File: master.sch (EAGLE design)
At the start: 27 parts, among them IC1 MEGA164/324/644/1284, SW1 CI-11, U2 3V3 something

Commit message: added forgotten lan interface
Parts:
- removed DHT22: FE04-1, con-lsta:FE04-1
- removed JP1: AVR-ISP-6VERT, avr-7:AVR-ISP-6VERT
- removed NRF24L01: (no value), con-lsta:FE05-2
- removed S1, S3: (no value), switch-omron:10-XX
- removed U$1: BTHQ24008VSS, lcd_displays:BTHQ24008VSS
- removed U2: 3V3 something, asko:MCP1702-5002
- added C10, C11, C12, C17, C18, C19, C20, C21, C4, C5, C6, C9: 100n, rcl:C-EUC0603
- added C13, C15: 10n, rcl:C-EUC0603
- added C14: .22, carrilib:SUPERCAP
- added C16: 10u, rcl:C-EUC0603
- added C22, C23: 22p, rcl:C-EUC0603
- added D1: BAS40-04, diode:BAS40-04
- added IC2: MCP1703-3302, karlnet-parts:MCP1700SOT89
- added IC3: ENC28J60SO, microchip:ENC28J60SO
- added L2: 10u, inductor-neosid:SM-NE29
- added LAN1: MAGJACK, magjack:MAGJACK
- added LCD1: LCD, external:LCD
- added M1: DHT22-NP, modules:DHT22-NP
- added M2: NRF24L01P-M, modules:NRF24L01P-M
- added PDI: AVR-PDIVERT, avr-7:AVR-PDIVERT
- added Q2: IRLML2502, mosfet:IRLML2502
- added Q3: 25MHz, crystal:CRYSTALHC49S
- added R10, R12: 49R9, rcl:R-EU_R0603
- added R11: 4k7, rcl:R-EU_R0603
- added R13: 2k, rcl:R-EU_R0603
- added R14, R15: 100, rcl:R-EU_R0603
- added R9: 10K, rcl:R-EU_R0603
- added U1: 25LC640A-E/SN, microchip:25LC640A-E/SN
- added UC1: XMEGA-A3TQFP, avr-7:XMEGA-A3TQFP
- added X1: serial, pinhead-mod:PINHD-1X4_2.54
- added X2: SPI/1W, con-amp-micromatch:MICROMATCH-8
- added X3: I2C, con-amp-micromatch:MICROMATCH-4
- added X4: ADC, con-amp-micromatch:MICROMATCH-8
- added X5: (no value), con-usb:USB-MB-S
- added X6, X7, X8, X9: PS25_3W-R, con_PS25:PS25_3W-R
- C1, C2, C3, C7, C8: device rcl:C-EUC0805 -> rcl:C-EUC0603
- IC1: value MEGA164/324/644/1284 -> DS1302SOIC; device avr-7:MEGA164P/324P/644P-PU -> adafruit:DS1302SOIC
- R1, R2, R4, R5: device rcl:R-EU_R0805 -> rcl:R-EU_R0603
- R3: value 10k -> 10K; device pot:TRIM_EU-ST10 -> rcl:R-EU_R0603
- R6, R7: value 4k7 -> 49R9; device rcl:R-EU_0207/7 -> rcl:R-EU_R0603
- R8: device rcl:R-EU_0207/7 -> rcl:R-EU_R0603
- S2: device switch-omron:10-XX -> jt-switches:MEC-SWITCHSMT
- SG1: value EFBAA40D101 -> RMP-14SP; device buzzer:EFBAA40D101 -> buzzer:F/CM12P
- SW1: value CI-11 -> EC12E_SW; device piher:CI-11 -> switch-alps:EC12E_SW
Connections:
- removed net !RESET: IC1.!RESET, JP1.5, R1.1
- removed net +3V3: C8.1, NRF24L01.10, NRF24L01.9, U2.OUT
- removed net PA0: IC1.(ADC0/PCINT0)PA0, U$1.RS
- removed net PA1: IC1.(ADC1/PCINT1)PA1, U$1.R/W
- removed net PA2: IC1.(ADC2/PCINT2)PA2, U$1.E
- removed net PA3: IC1.(ADC3/PCINT3)PA3, U$1.DB4
- removed net PA4: IC1.(ADC4/PCINT4)PA4, U$1.DB5
- removed net PA5: IC1.(ADC5/PCINT5)PA5, U$1.DB6
- removed net PA6: IC1.(ADC6/PCINT6)PA6, U$1.DB7
- removed net PA7: IC1.(ADC7/PCINT7)PA7, SG1.1
- removed net PB0: IC1.(XCK0/T0/PCINT8)PB0, R4.1
- removed net PB1: IC1.(CLKO/T1/PCINT9)PB1, R5.1
- removed net PB2: IC1.(INT2/AIN0/PCINT10)PB2, NRF24L01.4
- removed net PB3: IC1.(OC0A/AIN1/PCINT11)PB3, JP1.4, NRF24L01.7
- removed net PB4: IC1.(OC0B/!SS!/PCINT12)PB4, JP1.1, NRF24L01.8
- removed net PB5: IC1.(MOSI/PCINT13)PB5, JP1.3, R8.2
- removed net PB6: IC1.(MISO/PCINT14)PB6, R7.1
- removed net PB7: IC1.(SCK/PCINT15)PB7, R6.1
- removed net PC0: IC1.(SCL/PCINT16)PC0, SW1A.B
- removed net PC1: IC1.(SDA/PCINT17)PC1, SW1A.A
- removed net PC2: IC1.(TCK/PCINT18)PC2, SW1B.D
- removed net PC3: IC1.(TMS/PCINT19)PC3, S1.P
- removed net PC4: IC1.(TDO/PCINT20)PC4, S2.P
- removed net PC5: IC1.(TDI/PCINT21)PC5, S3.P
- removed net PD5: IC1.(OC1A/PCINT29)PD5, U$1.K
- removed net PD6: DHT22.2, IC1.(OC2B/ICP/PCINT30)PD6, R2.2
- new net !EEPCS: U1.!CS, UC1.PF0(OC0A)
- new net !EEPHOLD: U1.!HOLD, UC1.PF1(OC0B/XCK0)
- new net !LANCS: IC3.!CS, UC1.PC6(MISO/RXD1)
- new net !LANINT: IC3.!INT, UC1.PC5(OC1B/MOSI/XCK1)
- new net !RFCS: M2.!CS, UC1.PD1(OC0B/XCK0)
- new net ADC0: UC1.PA0(ADC0/AREFA), X4-2.S
- new net ADC1: UC1.PA1(ADC1), X4-3.S
- new net ADC2: UC1.PA2(ADC2), X4-4.S
- new net ADC3: UC1.PA3(ADC3), X4-5.S
- new net ADC4: UC1.PA4(ADC4), X4-6.S
- new net ADC5: UC1.PA5(ADC5), X4-7.S
- new net BUZZ: SG1.1, UC1.PF7
- new net DHTDATA: M1.DATA, R2.1, UC1.PA7/(ADC7/AC0-OUT)
- new net LCD_BGLED: Q2.G, R9.1, UC1.PC1(OC0B/XCK0/SCL)
- new net LCD_CONTR: C11.1, UC1.PC0(OC0A/SDA)
- new net LCD_D4: LCD1.DB4, UC1.PB4(ADC4/TMS), X8-1.P$1
- new net LCD_D5: LCD1.DB5, UC1.PB5(ADC5/TDI), X8-2.P$1
- new net LCD_D6: LCD1.DB6, UC1.PB6(ADC6/TCK), X8-3.P$1
- new net LCD_D7: LCD1.DB7, UC1.PB7(ADC7/AC0-OUT/TDO), X9-1.P$1
- new net LCD_E: LCD1.E, UC1.PB3(ADC3/DAC1), X7-3.P$1
- new net LCD_RS: LCD1.RS, UC1.PB1(ADC1), X7-1.P$1
- new net LCR_RW: LCD1.R/W, UC1.PB2(ADC2/DAC0), X7-2.P$1
- new net LED1: LED1.A, UC1.PA6(ADC6)
- new net LED2: LED2.A, UC1.PB0(ADC0/AREFB)
- new net MISO: IC3.SO, M2.MISO, U1.SO, UC1.PE6(RSC1/MISO/TOSC2), X2-5.S
- new net MOSI: IC3.SI, M2.MOSI, U1.SI, UC1.PE5(OC1B/SCK1/MOSI), X2-6.S
- new net N$10: PDI.1, UC1.PDI-DATA
- new net N$11: PDI.5, R1.1, UC1.PDI-CLK/!RESET
- new net N$12: IC3.TPIN-, LAN1-JACK.RD-, R12.1
- new net N$14: IC3.TPOUT+, LAN1-JACK.TD+, R7.2
- new net N$15: C6.1, L2.1, UC1.AVCC
- new net N$16: C15.1, R10.2, R12.2
- new net N$17: IC3.RBIAS, R13.1
- new net N$18: C23.1, IC3.OSC2, Q3.1
- new net N$19: C22.1, IC3.OSC1, Q3.2
- new net N$20: C16.1, IC3.VCAP
- new net N$21: IC3.LEDA, LAN1-GR.A
- new net N$22: IC3.LEDB, LAN1-YE.A
- new net N$23: LAN1-GR.C, R14.1
- new net N$24: LAN1-YE.C, R15.1
- new net N$8: LCD1.K, Q2.D, X9-3.P$1
- new net RFCE: M2.CE, UC1.PD2(OC0C/RXD0)
- new net RFIRQ: M2.IRQ, UC1.PD0(OC0A)
- new net RTC_CE: IC1.CE, UC1.PE4(OC1A/!SS!)
- new net RTC_CLK: IC1.SCLK, UC1.PE2(OC0C/RXD0)
- new net RTC_IO: IC1.I/O, UC1.PE3(OC0D/TXD0)
- new net RXD: UC1.PF2(OC0C/RXD0), X1.2
- new net S1A: SW1G$1.A, UC1.PC7(SCK/TXD1/CLKO/EVO)
- new net S1B: SW1G$1.B, UC1.PC4(OC1A/!SS!)
- new net S1P: SW1G$2.2, UC1.PC3(OC0D/TXD0)
- new net S2: S2.A1, UC1.PC2(OC0C/RXD0)
- new net SCK: IC3.SCK, M2.SCK, U1.SCK, UC1.PE7(TSD1/SCK/CLKO/EVO/TOSC1), X2-7.S
- new net SCL: R11.2, UC1.PE1(OC0B/XCK0/SCL), X3-3.S
- new net SDA: R8.2, UC1.PE0(OC0A/SDA), X3-2.S
- new net SS1WA: UC1.PD5(OC1B/XCK1/MOSI), X2-2.S
- new net SS1WB: UC1.PD4(OC1A/!SS!), X2-4.S
- new net TXD: UC1.PF3(OC0D/TXD0), X1.3
- new net USBD_N: UC1.PD6(RXD1/MISO), X5.D-
- new net USBD_P: UC1.PD7(TXD1/SCK/CLKO/EVO), X5.D+
- new net VCC: C1.1, C12.1, C13.1, C17.1, C18.1, C19.1, C2.1, C20.1, C21.1, C3.1, C4.1, C5.1, C8.1, C9.2, IC1.VCC, IC2.OUT, IC3.VDD, IC3.VDDOSC, IC3.VDDPLL, IC3.VDDRX, IC3.VDDTX, L2.2, LAN1-JACK.TCT, LCD1.VDD, M1.VCC, M2.VCC, PDI.2, R1.2, R11.1, R2.2, R6.1, R7.1, R8.1, U1.VCC, UC1.VCC@1, UC1.VCC@2, UC1.VCC@3, UC1.VCC@4, UC1.VCC@5, X1.1, X2-1.S, X3-1.S, X4-1.S, X6-2.P$1
- net +5V: now also IC2.IN, LCD1.A, X5.VBUS, X9-2.P$1; no longer C1.1, C2.1, C3.2, DHT22.1, IC1.AVCC, IC1.VCC, JP1.2, R1.2, R2.1, R3.A, U$1.A, U$1.VDD, U2.IN
- net GND: now also C10.1, C12.2, C13.2, C14.P$2, C15.2, C16.2, C17.2, C18.2, C19.2, C2.2, C20.2, C21.2, C22.2, C23.2, C3.2, C4.2, C5.2, C6.2, C9.1, D1.C2, IC1.GND, IC2.GND, IC3.VSS, IC3.VSSOSC, IC3.VSSPLL, IC3.VSSRX, IC3.VSSTX, LAN1-JACK.GND, LCD1.VSS, M1.GND, M2.GND, PDI.6, Q2.S, R13.2, R14.2, R15.2, R3.1, R4.2, R5.2, R9.2, S2.B1, S2.B2, SW1G$1.C, SW1G$2.1, U1.!WP, U1.VSS, UC1.GND@1, UC1.GND@2, UC1.GND@3, UC1.GND@4, UC1.GND@5, UC1.GND@6, X1.4, X2-3.S, X2-8.S, X3-4.S, X4-8.S, X5.GND, X6-1.P$1; no longer C3.1, DHT22.4, IC1.GND@1, IC1.GND@2, JP1.6, LED1.C, LED2.C, NRF24L01.1, NRF24L01.2, R3.E, S1.S, S1.S1, S2.S, S2.S1, S3.S, S3.S1, SW1A.C, SW1B.E, U$1.VSS, U2.GND
- net N$1: now also IC1.X1, Q1.2; no longer C2.2, IC1.AREF
- net N$13: now also IC3.TPOUT-, LAN1-JACK.TD-, R6.2; no longer LED1.A, R4.2
- net N$2: now also LED1.C, R4.1; no longer LED2.A, R5.2
- net N$3: now also IC1.X2; no longer IC1.(TOSC2/PCINT23)PC7
- net N$4: now also C11.2, D1.C1A2; no longer IC1.(TOSC1/PCINT22)PC6, Q1.2
- net N$5: now also LED2.C, R5.1; no longer NRF24L01.5, R6.2
- net N$6: now also C14.P$1, IC1.VBAT; no longer NRF24L01.3, R7.2
- net N$7: now also IC3.TPIN+, LAN1-JACK.RD+, R10.1; no longer NRF24L01.6, R8.1
- net N$9: now also C10.2, D1.A1, LCD1.VO, R3.2, X6-3.P$1; no longer R3.S, U$1.VO
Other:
- note removed: "CE"
- note removed: "CSN"
- note removed: "DATA"
- note removed: "GND"
- note removed: "IRQ"
- note removed: "MISO"
- note removed: "MOSI"
- note removed: "NC"
- note removed: "SCK"
- note removed: "VCC"

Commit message: improved spacing between some layers
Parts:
- removed UC1: XMEGA-A3TQFP, avr-7:XMEGA-A3TQFP
- added U3: 25LC640A-E/SN, microchip:25LC640A-E/SN
- Q1: value (none) -> IRLML2502; device crystal:CRYSTALTC26H -> mosfet:IRLML2502
- Q2: value IRLML2502 -> (none); device mosfet:IRLML2502 -> crystal:CRYSTALTC26H
- SW1: value EC12E_SW -> EC11E_SW; device switch-alps:EC12E_SW -> switch-alps:EC11E_SW
- U1: value 25LC640A-E/SN -> XMEGA-A3TQFP; device microchip:25LC640A-E/SN -> avr-7:XMEGA-A3TQFP
- renumbered IC1 to U2, IC3 to U4, L2 to L1
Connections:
- net !EEPCS: now also U1.PF0(OC0A), U3.!CS; no longer U1.!CS, UC1.PF0(OC0A)
- net !EEPHOLD: now also U1.PF1(OC0B/XCK0), U3.!HOLD; no longer U1.!HOLD, UC1.PF1(OC0B/XCK0)
- net !LANCS: now also U1.PC6(MISO/RXD1); no longer UC1.PC6(MISO/RXD1)
- net !LANINT: now also U1.PC5(OC1B/MOSI/XCK1); no longer UC1.PC5(OC1B/MOSI/XCK1)
- net !RFCS: now also U1.PD1(OC0B/XCK0); no longer UC1.PD1(OC0B/XCK0)
- net ADC0: now also U1.PA0(ADC0/AREFA); no longer UC1.PA0(ADC0/AREFA)
- net ADC1: now also U1.PA1(ADC1); no longer UC1.PA1(ADC1)
- net ADC2: now also U1.PA2(ADC2); no longer UC1.PA2(ADC2)
- net ADC3: now also U1.PA3(ADC3); no longer UC1.PA3(ADC3)
- net ADC4: now also U1.PA4(ADC4); no longer UC1.PA4(ADC4)
- net ADC5: now also U1.PA5(ADC5); no longer UC1.PA5(ADC5)
- net BUZZ: now also U1.PF7; no longer UC1.PF7
- net DHTDATA: now also U1.PA7/(ADC7/AC0-OUT); no longer UC1.PA7/(ADC7/AC0-OUT)
- net GND: now also Q1.S, SW1G$3.G, SW1G$4.G, U1.GND@1, U1.GND@2, U1.GND@3, U1.GND@4, U1.GND@5, U1.GND@6, U3.!WP, U3.VSS; no longer Q2.S, U1.!WP, U1.VSS, UC1.GND@1, UC1.GND@2, UC1.GND@3, UC1.GND@4, UC1.GND@5, UC1.GND@6
- net LCD_BGLED: now also Q1.G, U1.PC1(OC0B/XCK0/SCL); no longer Q2.G, UC1.PC1(OC0B/XCK0/SCL)
- net LCD_CONTR: now also U1.PC0(OC0A/SDA); no longer UC1.PC0(OC0A/SDA)
- net LCD_D4: now also U1.PB4(ADC4/TMS); no longer UC1.PB4(ADC4/TMS)
- net LCD_D5: now also U1.PB5(ADC5/TDI); no longer UC1.PB5(ADC5/TDI)
- net LCD_D6: now also U1.PB6(ADC6/TCK); no longer UC1.PB6(ADC6/TCK)
- net LCD_D7: now also U1.PB7(ADC7/AC0-OUT/TDO); no longer UC1.PB7(ADC7/AC0-OUT/TDO)
- net LCD_E: now also U1.PB3(ADC3/DAC1); no longer UC1.PB3(ADC3/DAC1)
- net LCD_RS: now also U1.PB1(ADC1); no longer UC1.PB1(ADC1)
- net LCR_RW: now also U1.PB2(ADC2/DAC0); no longer UC1.PB2(ADC2/DAC0)
- net LED1: now also U1.PA6(ADC6); no longer UC1.PA6(ADC6)
- net LED2: now also U1.PB0(ADC0/AREFB); no longer UC1.PB0(ADC0/AREFB)
- net MISO: now also U1.PE6(RSC1/MISO/TOSC2), U3.SO; no longer U1.SO, UC1.PE6(RSC1/MISO/TOSC2)
- net MOSI: now also U1.PE5(OC1B/SCK1/MOSI), U3.SI; no longer U1.SI, UC1.PE5(OC1B/SCK1/MOSI)
- net N$1: now also Q2.2; no longer Q1.2
- net N$10: now also U1.PDI-DATA; no longer UC1.PDI-DATA
- net N$11: now also U1.PDI-CLK/!RESET; no longer UC1.PDI-CLK/!RESET
- net N$15: now also U1.AVCC; no longer UC1.AVCC
- net N$3: now also Q2.1; no longer Q1.1
- net N$8: now also Q1.D; no longer Q2.D
- net RFCE: now also U1.PD2(OC0C/RXD0); no longer UC1.PD2(OC0C/RXD0)
- net RFIRQ: now also U1.PD0(OC0A); no longer UC1.PD0(OC0A)
- net RTC_CE: now also U1.PE4(OC1A/!SS!); no longer UC1.PE4(OC1A/!SS!)
- net RTC_CLK: now also U1.PE2(OC0C/RXD0); no longer UC1.PE2(OC0C/RXD0)
- net RTC_IO: now also U1.PE3(OC0D/TXD0); no longer UC1.PE3(OC0D/TXD0)
- net RXD: now also U1.PF2(OC0C/RXD0); no longer UC1.PF2(OC0C/RXD0)
- net S1A: now also U1.PC7(SCK/TXD1/CLKO/EVO); no longer UC1.PC7(SCK/TXD1/CLKO/EVO)
- net S1B: now also U1.PC4(OC1A/!SS!); no longer UC1.PC4(OC1A/!SS!)
- net S1P: now also U1.PC3(OC0D/TXD0); no longer UC1.PC3(OC0D/TXD0)
- net S2: now also U1.PC2(OC0C/RXD0); no longer UC1.PC2(OC0C/RXD0)
- net SCK: now also U1.PE7(TSD1/SCK/CLKO/EVO/TOSC1), U3.SCK; no longer U1.SCK, UC1.PE7(TSD1/SCK/CLKO/EVO/TOSC1)
- net SCL: now also U1.PE1(OC0B/XCK0/SCL); no longer UC1.PE1(OC0B/XCK0/SCL)
- net SDA: now also U1.PE0(OC0A/SDA); no longer UC1.PE0(OC0A/SDA)
- net SS1WA: now also U1.PD5(OC1B/XCK1/MOSI); no longer UC1.PD5(OC1B/XCK1/MOSI)
- net SS1WB: now also U1.PD4(OC1A/!SS!); no longer UC1.PD4(OC1A/!SS!)
- net TXD: now also U1.PF3(OC0D/TXD0); no longer UC1.PF3(OC0D/TXD0)
- net USBD_N: now also U1.PD6(RXD1/MISO); no longer UC1.PD6(RXD1/MISO)
- net USBD_P: now also U1.PD7(TXD1/SCK/CLKO/EVO); no longer UC1.PD7(TXD1/SCK/CLKO/EVO)
- net VCC: now also U1.VCC@1, U1.VCC@2, U1.VCC@3, U1.VCC@4, U1.VCC@5, U3.VCC; no longer U1.VCC, UC1.VCC@1, UC1.VCC@2, UC1.VCC@3, UC1.VCC@4, UC1.VCC@5

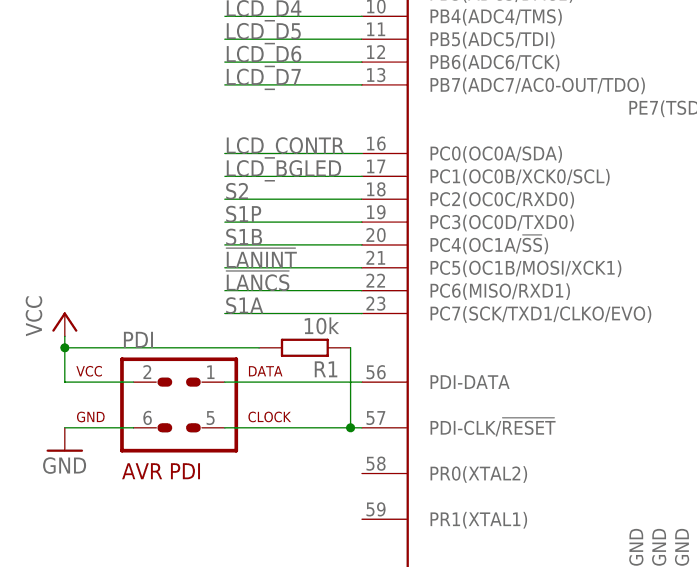
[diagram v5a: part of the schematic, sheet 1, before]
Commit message: quadrature decoder needs two successive pins for input -> swapped s1
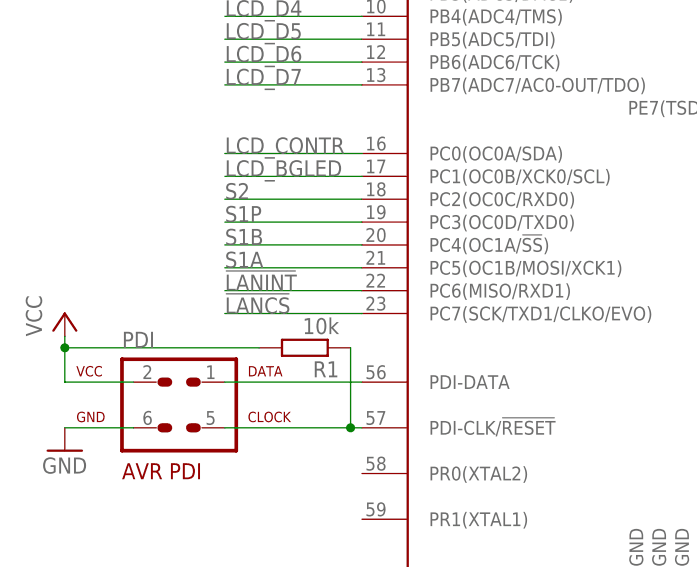
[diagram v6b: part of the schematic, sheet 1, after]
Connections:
- net !LANCS: now also U1.PC7(SCK/TXD1/CLKO/EVO); no longer U1.PC6(MISO/RXD1)
- net !LANINT: now also U1.PC6(MISO/RXD1); no longer U1.PC5(OC1B/MOSI/XCK1)
- net S1A: now also U1.PC5(OC1B/MOSI/XCK1); no longer U1.PC7(SCK/TXD1/CLKO/EVO)
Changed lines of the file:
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@@
-</segment>
-</net>
-<net name="S1A" class="0">
-<segment>
-<pinref part="U1" gate="G$1" pin="PC7(SCK/TXD1/CLKO/EVO)"/>
-<wire x1="41.91" y1="49.53" x2="26.67" y2="49.53" width="0.1524" layer="91"/>
-<label x="26.67" y="49.53" size="1.778" layer="95"/>
 </segment>
 </net>
@@
 </segment>
 </net>
-<net name="!LANINT" class="0">
+<net name="S1A" class="0">
 <segment>
 <pinref part="U1" gate="G$1" pin="PC5(OC1B/MOSI/XCK1)"/>
@@
 </segment>
 </net>
-<net name="!LANCS" class="0">
+<net name="!LANINT" class="0">
 <segment>
 <label x="26.67" y="52.07" size="1.778" layer="95"/>
@@
 </segment>
 </net>
+<net name="!LANCS" class="0">
+<segment>
+<pinref part="U1" gate="G$1" pin="PC7(SCK/TXD1/CLKO/EVO)"/>
+<wire x1="41.91" y1="49.53" x2="26.67" y2="49.53" width="0.1524" layer="91"/>
+<label x="26.67" y="49.53" size="1.778" layer="95"/>
+</segment>
+</net>
